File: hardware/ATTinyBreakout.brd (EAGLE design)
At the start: 25.4 x 38.1 mm, 16 parts, among them U1 TINY85-20-DIP

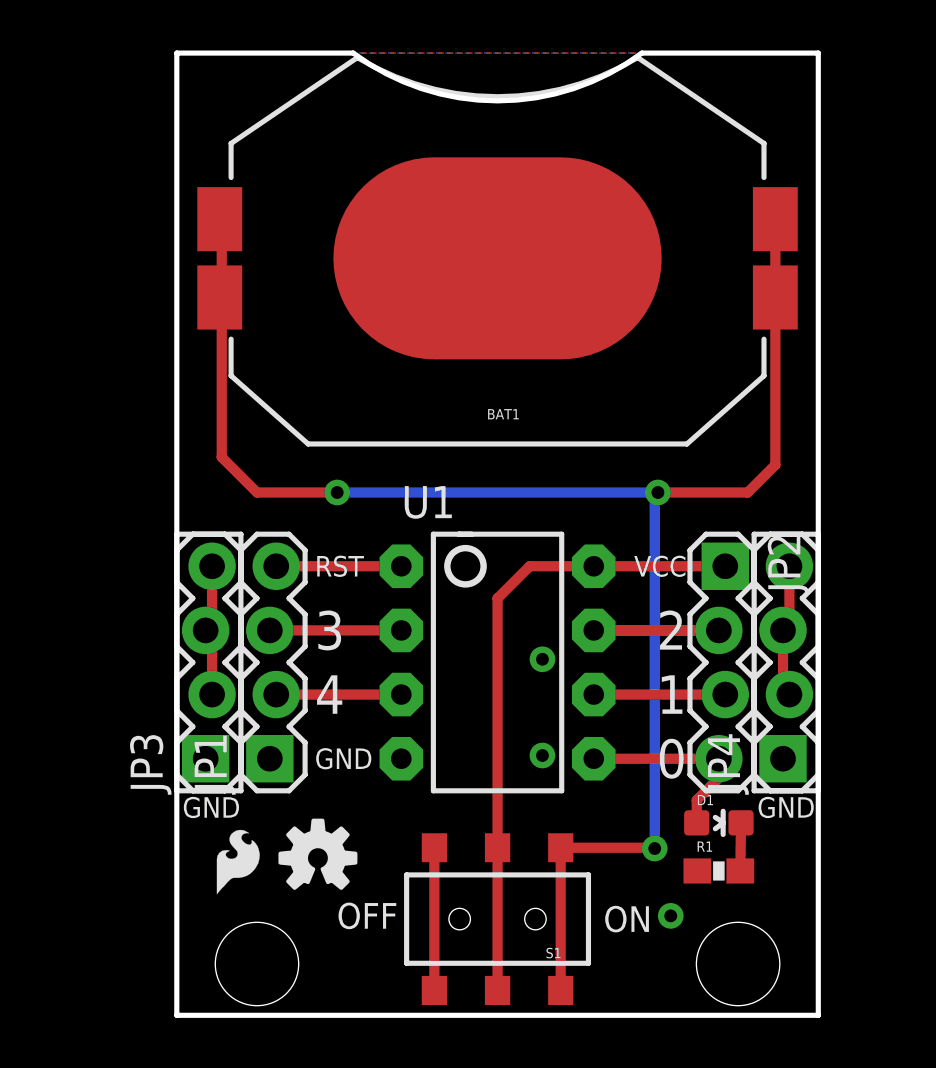
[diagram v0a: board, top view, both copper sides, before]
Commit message: Revision with 3 pin headers (Ludus style)
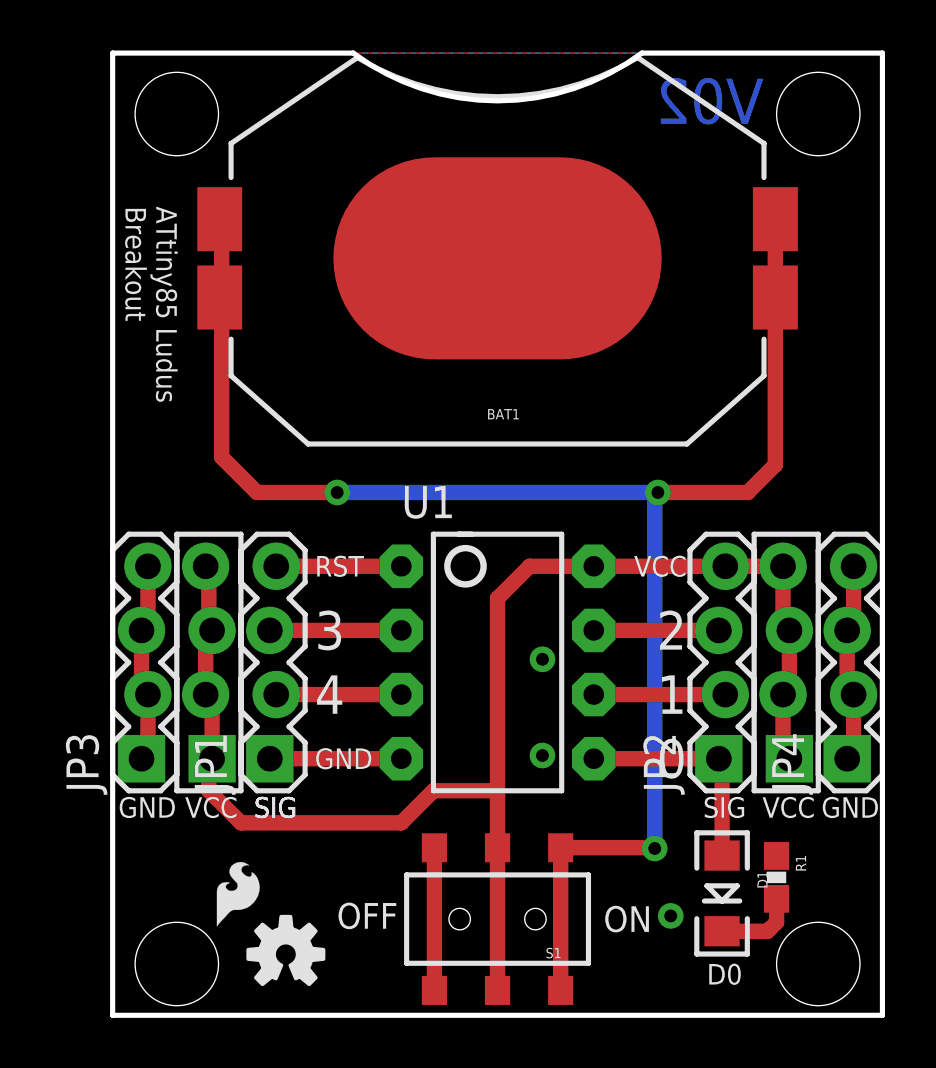
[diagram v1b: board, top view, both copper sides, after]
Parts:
- added JP5, JP6: (no value), SparkFun-Connectors:1X04_LOCK
- added STANDOFF3, STANDOFF4: STAND-OFF, SparkFun-Electromechanical:STAND-OFF
- added U$2: SFE_LUDUSSFE_LUDUS-M, SparkFun-Aesthetics:SFE_LUDUS-M
- D1: device SparkFun-LED:LED-0603 -> SparkFun-LED:LED-1206
- moved FRAME1 25.0 mm to (10.2, -35.6)
- moved JP2 7.62 mm to (24.1, 10.2), turned to 90 degrees
- moved LOGO3 4.02 mm to (6.86, 2.41)
- moved STANDOFF1 3.18 mm to (27.9, 2.03)
- moved STANDOFF2 3.17 mm to (2.54, 2.03)
- moved D1 2.80 mm to (24.1, 4.83)
- moved JP3 2.54 mm to (1.27, 10.2)
- moved JP4 2.54 mm to (29.2, 10.2)
- moved R1 2.30 mm to (26.3, 5.46), turned to 270 degrees
- moved LOGO2 1.27 mm to (3.81, 3.17)
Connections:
- removed net SWITCHED_VCC: JP2.1, S1.2, S1.5, U1.8
- new net N$3: JP2.4, JP5.1, JP5.2, JP5.3, JP5.4, JP6.1, JP6.2, JP6.3, JP6.4, S1.2, S1.5, U1.8
- net PB0_MOSI: now also JP2.1; no longer JP2.4
- net PB1_MISO: now also JP2.2; no longer JP2.3
- net PB2_SCK: now also JP2.3; no longer JP2.2
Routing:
- net N$3: track 0.00 -> 57.3 mm
- net SWITCHED_VCC: track 25.1 -> 0.00 mm
- net GND: track 10.7 -> 21.2 mm
- net PB2_SCK: track 9.91 -> 4.95 mm
- net N$1: track 1.91 -> 3.23 mm
- net PB0_MOSI: track 7.86 -> 8.84 mm
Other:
- board size 25.4 x 38.1 mm -> 30.5 x 38.1 mm
- board text added: "ATTiny85 Ludus Breakout"
- board text added: "ATtiny85 Ludus Breakout"
- board text added: "D0"
- board text added: "SIG"
- board text added: "V02"
- board text removed: "ATTiny85 Battery Breakout"
